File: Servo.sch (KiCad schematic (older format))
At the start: 2 parts, among them P2 CONN_01X03, P3 CONN_01X03

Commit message: añaadido zocalo para sensor de temperatura y primera distribucion sobre la PCB
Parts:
- P2, P3: footprint (none) -> Pin_Headers:Pin_Header_Straight_1x03
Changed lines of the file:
@@
 $Descr User 8268 5846
 encoding utf-8
-Sheet 10 13
+Sheet 10 14
 Title ""
 Date ""
@@
 F 0 "P2" H 2878 2241 50  0000 L CNN
 F 1 "CONN_01X03" H 2878 2150 50  0000 L CNN
-F 2 "" H 2800 2200 50  0000 C CNN
+F 2 "Pin_Headers:Pin_Header_Straight_1x03" H 2800 2200 50  0001 C CNN
 F 3 "" H 2800 2200 50  0000 C CNN
 	1    2800 2200
@@
 F 0 "P3" H 2878 2941 50  0000 L CNN
 F 1 "CONN_01X03" H 2878 2850 50  0000 L CNN
-F 2 "" H 2800 2900 50  0000 C CNN
+F 2 "Pin_Headers:Pin_Header_Straight_1x03" H 2800 2900 50  0001 C CNN
 F 3 "" H 2800 2900 50  0000 C CNN
 	1    2800 2900
@@
 $EndComp
 $Comp
-L +5V #PWR037
+L +5V #PWR039
 U 1 1 5794EAD6
 P 2350 1750
-F 0 "#PWR037" H 2350 1600 50  0001 C CNN
+F 0 "#PWR039" H 2350 1600 50  0001 C CNN
 F 1 "+5V" H 2365 1923 50  0000 C CNN
 F 2 "" H 2350 1750 50  0000 C CNN
@@
 $EndComp
 $Comp
-L GND #PWR038
+L GND #PWR040
 U 1 1 5794EAEE
 P 2450 3350
-F 0 "#PWR038" H 2450 3100 50  0001 C CNN
+F 0 "#PWR040" H 2450 3100 50  0001 C CNN
 F 1 "GND" H 2455 3177 50  0000 C CNN
 F 2 "" H 2450 3350 50  0000 C CNN

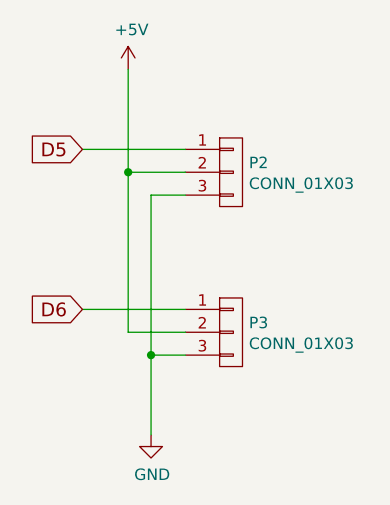
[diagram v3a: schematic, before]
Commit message: ordenar referencias de componentes
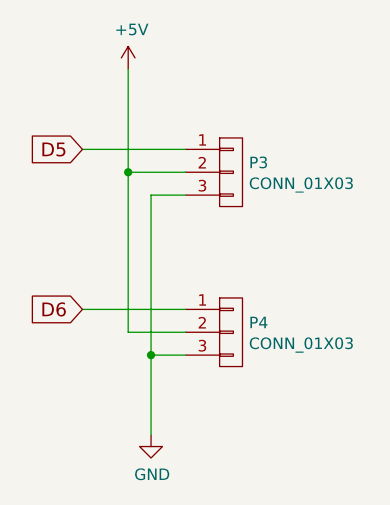
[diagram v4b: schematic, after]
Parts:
- P3: renamed from P2; Fabricante (none) -> TE CONNECTIVITY; Provedor (none) -> TME; Ref (none) -> 4-103321-8; Ref_Proveedor (none) -> 4-103321-8
- P4: renamed from P3; Fabricante (none) -> TE CONNECTIVITY; Provedor (none) -> TME; Ref (none) -> 4-103321-8; Ref_Proveedor (none) -> 4-103321-8
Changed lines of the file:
@@
 $Descr User 8268 5846
 encoding utf-8
-Sheet 10 15
+Sheet 6 15
 Title ""
 Date ""
@@
 $EndDescr
 $Comp
-L CONN_01X03 P2
+L CONN_01X03 P3
 U 1 1 5794EA47
 P 2800 2200
-F 0 "P2" H 2878 2241 50  0000 L CNN
+F 0 "P3" H 2878 2241 50  0000 L CNN
 F 1 "CONN_01X03" H 2878 2150 50  0000 L CNN
 F 2 "Pin_Headers:Pin_Header_Straight_1x03" H 2800 2200 50  0001 C CNN
 F 3 "" H 2800 2200 50  0000 C CNN
+F 4 "TE CONNECTIVITY" H 2800 2200 60  0001 C CNN "Fabricante"
+F 5 "4-103321-8" H 2800 2200 60  0001 C CNN "Ref"
+F 6 "~" H 2800 2200 60  0001 C CNN "Potencia"
+F 7 "~" H 2800 2200 60  0001 C CNN "Tolerancia"
+F 8 "TME" H 2800 2200 60  0001 C CNN "Provedor"
+F 9 "4-103321-8" H 2800 2200 60  0001 C CNN "Ref_Proveedor"
 	1    2800 2200
 	1    0    0    -1
 $EndComp
 $Comp
-L CONN_01X03 P3
+L CONN_01X03 P4
 U 1 1 5794EAA8
 P 2800 2900
-F 0 "P3" H 2878 2941 50  0000 L CNN
+F 0 "P4" H 2878 2941 50  0000 L CNN
 F 1 "CONN_01X03" H 2878 2850 50  0000 L CNN
 F 2 "Pin_Headers:Pin_Header_Straight_1x03" H 2800 2900 50  0001 C CNN
 F 3 "" H 2800 2900 50  0000 C CNN
+F 4 "TE CONNECTIVITY" H 2800 2900 60  0001 C CNN "Fabricante"
+F 5 "4-103321-8" H 2800 2900 60  0001 C CNN "Ref"
+F 6 "~" H 2800 2900 60  0001 C CNN "Potencia"
+F 7 "~" H 2800 2900 60  0001 C CNN "Tolerancia"
+F 8 "TME" H 2800 2900 60  0001 C CNN "Provedor"
+F 9 "4-103321-8" H 2800 2900 60  0001 C CNN "Ref_Proveedor"
 	1    2800 2900
 	1    0    0    -1
 $EndComp
 $Comp
-L +5V #PWR032
+L +5V #PWR18
 U 1 1 5794EAD6
 P 2350 1750
-F 0 "#PWR032" H 2350 1600 50  0001 C CNN
+F 0 "#PWR18" H 2350 1600 50  0001 C CNN
 F 1 "+5V" H 2365 1923 50  0000 C CNN
 F 2 "" H 2350 1750 50  0000 C CNN
@@
 $EndComp
 $Comp
-L GND #PWR033
+L GND #PWR19
 U 1 1 5794EAEE
 P 2450 3350
-F 0 "#PWR033" H 2450 3100 50  0001 C CNN
+F 0 "#PWR19" H 2450 3100 50  0001 C CNN
 F 1 "GND" H 2455 3177 50  0000 C CNN
 F 2 "" H 2450 3350 50  0000 C CNN

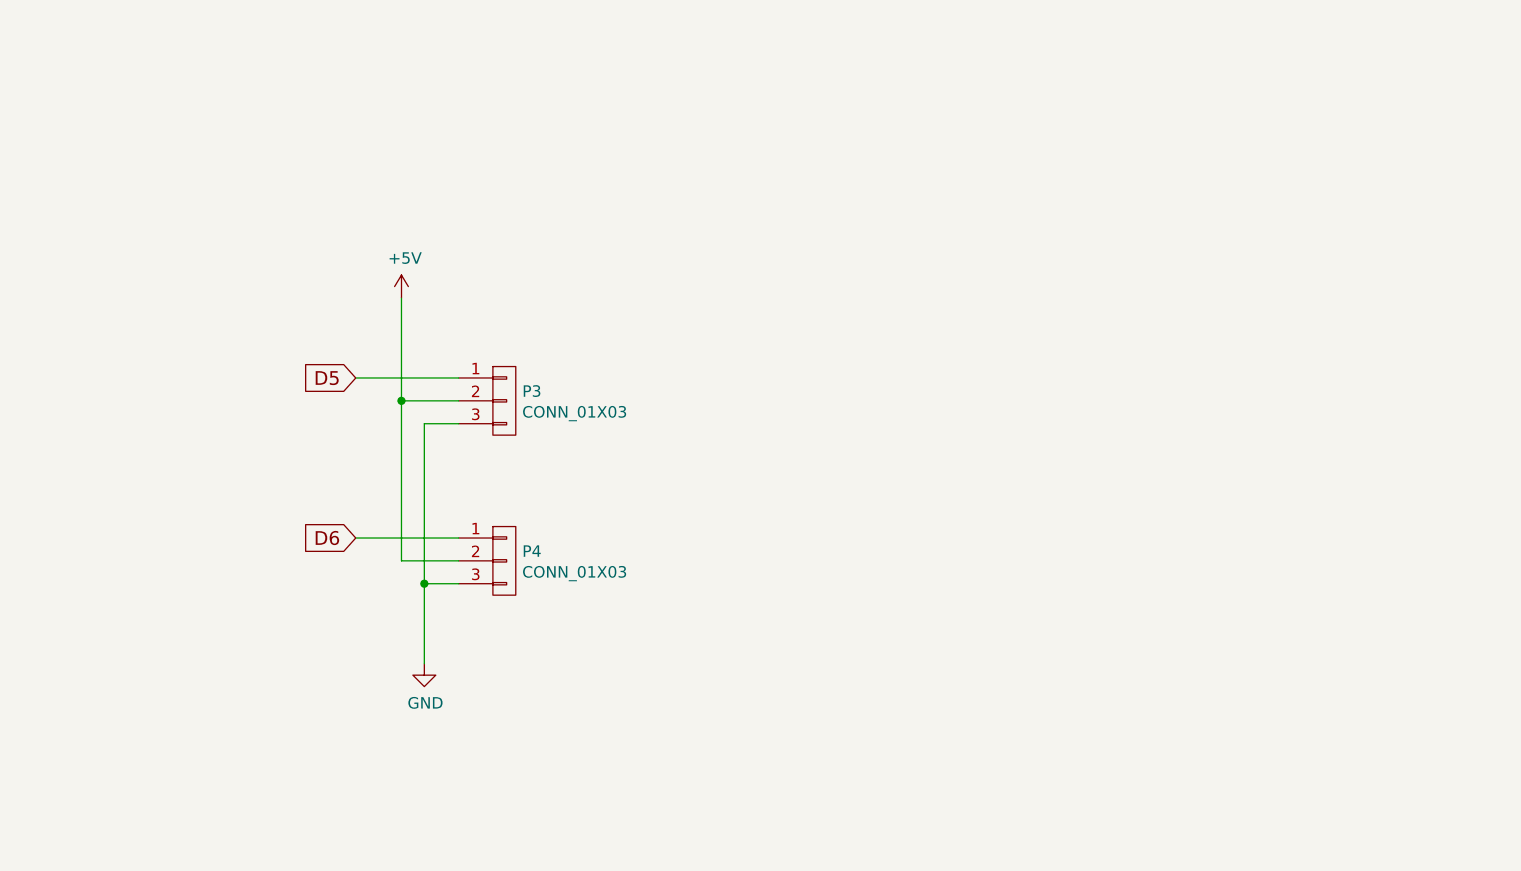
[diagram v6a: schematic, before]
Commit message: añadidos driver para led y conectores para fotodiodos infrarrojos
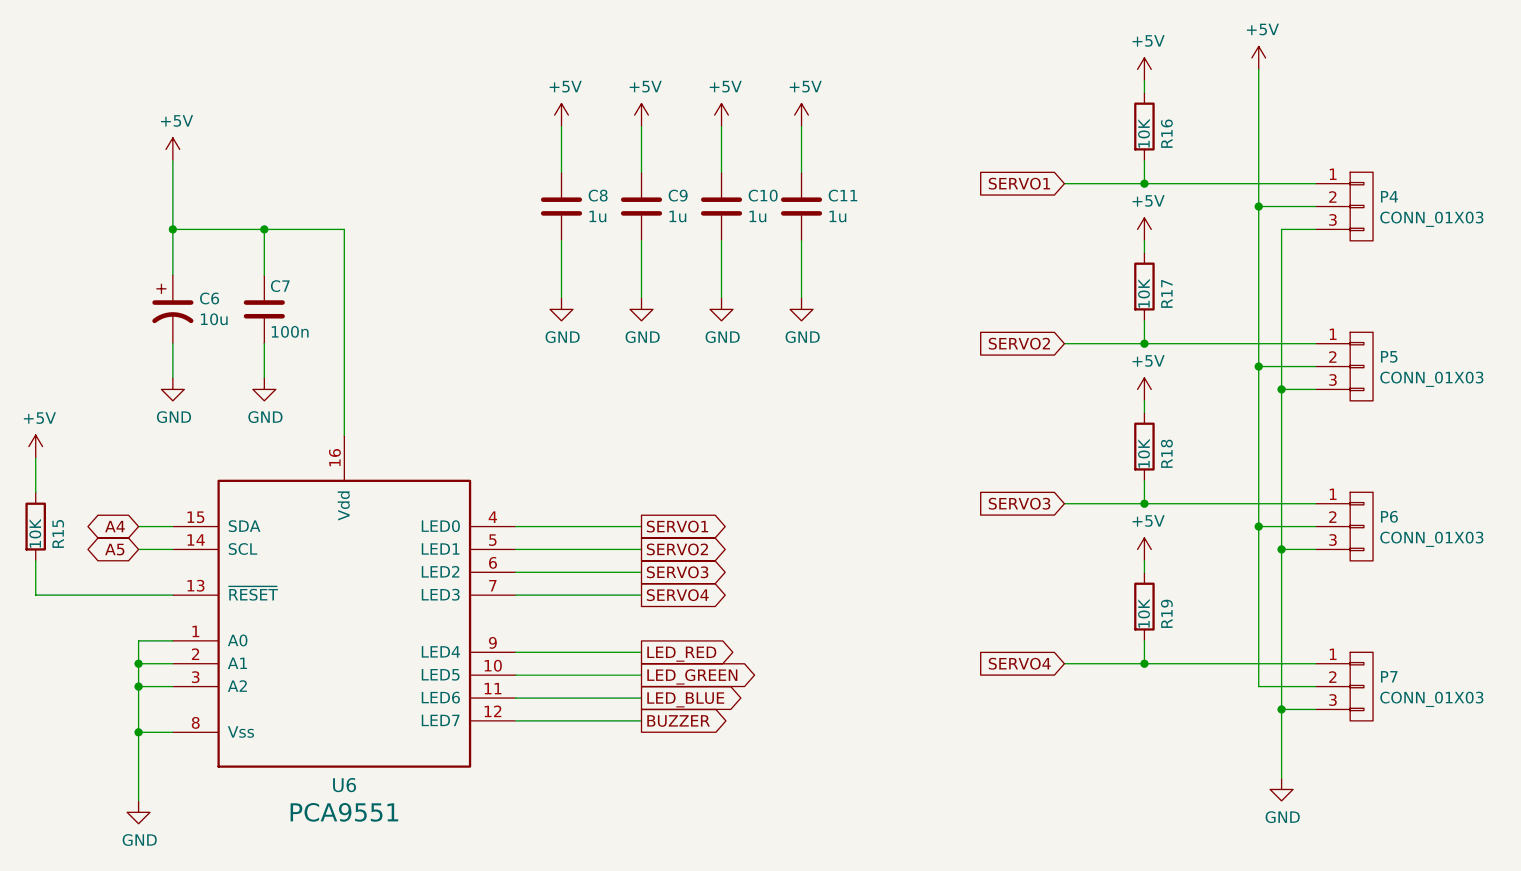
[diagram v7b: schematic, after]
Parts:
- added C10, C11, C8, C9: 1u, Capacitors_SMD:C_0805, symbol C
- added C6: 10u, Capacitors_Tantalum_SMD:Tantalum_Case-A_EIA-3216-18_Reflow, symbol CP1
- added C7: 100n, Capacitors_SMD:C_0805, symbol C
- added P6, P7: CONN_01X03, Pin_Headers:Pin_Header_Straight_1x03, symbol CONN_01X03
- added R15, R16, R17, R18, R19: 10K, Resistencias:R_0805, symbol R
- added U6: PCA9551, Housings_SSOP:TSSOP-16_4.4x5mm_Pitch0.65mm, symbol PCA9551
- renumbered P3 to P4, P4 to P5
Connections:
- net +5V: now also C10.1, C11.1, C6.1, C7.1, C8.1, C9.1, P6.2 (P2), P7.2 (P2), R15.1, R16.1, R17.1, R18.1, R19.1, U6.16 (Vdd)
- net GND: now also C10.2, C11.2, C6.2, C7.2, C8.2, C9.2, P6.3 (P3), P7.3 (P3), U6.1 (A0), U6.2 (A1), U6.3 (A2), U6.8 (Vss)
- net D5 renamed SERVO1
- net SERVO1: now also R16.2, U6.4 (LED0)
- net D6 renamed SERVO2
- net SERVO2: now also R17.2, U6.5 (LED1)
- new net: R15.2, U6.13 (~RESET)
- new net A4: U6.15 (SDA)
- new net A5: U6.14 (SCL)
- new net BUZZER: U6.12 (LED7)
- new net LED_BLUE: U6.11 (LED6)
- new net LED_GREEN: U6.10 (LED5)
- new net LED_RED: U6.9 (LED4)
- new net SERVO3: P6.1 (P1), R18.2, U6.6 (LED2)
- new net SERVO4: P7.1 (P1), R19.2, U6.7 (LED3)
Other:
- moved on the sheet: P4, P5

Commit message: finalizado enrutado provisional
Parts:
- removed C6: 10u, Capacitors_Tantalum_SMD:Tantalum_Case-A_EIA-3216-18_Reflow, symbol CP1
- P4, P5, P6, P7: footprint Pin_Headers:Pin_Header_Straight_1x03 -> Pin_Headers:Pin_Header_Straight_1x03_Pitch2.54mm
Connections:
- net LED_BLUE: now also U6.10 (LED5); no longer U6.11 (LED6)
- net LED_GREEN: now also U6.11 (LED6); no longer U6.10 (LED5)
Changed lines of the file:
@@
 F 0 "P4" H 6628 1391 50  0000 L CNN
 F 1 "CONN_01X03" H 6628 1300 50  0000 L CNN
-F 2 "Pin_Headers:Pin_Header_Straight_1x03" H 6550 1350 50  0001 C CNN
+F 2 "Pin_Headers:Pin_Header_Straight_1x03_Pitch2.54mm" H 6550 1350 50  0001 C CNN
 F 3 "" H 6550 1350 50  0000 C CNN
 F 4 "TE CONNECTIVITY" H 6550 1350 60  0001 C CNN "Fabricante"
@@
 F 0 "P5" H 6628 2091 50  0000 L CNN
 F 1 "CONN_01X03" H 6628 2000 50  0000 L CNN
-F 2 "Pin_Headers:Pin_Header_Straight_1x03" H 6550 2050 50  0001 C CNN
+F 2 "Pin_Headers:Pin_Header_Straight_1x03_Pitch2.54mm" H 6550 2050 50  0001 C CNN
 F 3 "" H 6550 2050 50  0000 C CNN
 F 4 "TE CONNECTIVITY" H 6550 2050 60  0001 C CNN "Fabricante"
@@
 F 0 "P6" H 6628 2791 50  0000 L CNN
 F 1 "CONN_01X03" H 6628 2700 50  0000 L CNN
-F 2 "Pin_Headers:Pin_Header_Straight_1x03" H 6550 2750 50  0001 C CNN
+F 2 "Pin_Headers:Pin_Header_Straight_1x03_Pitch2.54mm" H 6550 2750 50  0001 C CNN
 F 3 "" H 6550 2750 50  0000 C CNN
 F 4 "TE CONNECTIVITY" H 6550 2750 60  0001 C CNN "Fabricante"
@@
 F 0 "P7" H 6628 3491 50  0000 L CNN
 F 1 "CONN_01X03" H 6628 3400 50  0000 L CNN
-F 2 "Pin_Headers:Pin_Header_Straight_1x03" H 6550 3450 50  0001 C CNN
+F 2 "Pin_Headers:Pin_Header_Straight_1x03_Pitch2.54mm" H 6550 3450 50  0001 C CNN
 F 3 "" H 6550 3450 50  0000 C CNN
 F 4 "TE CONNECTIVITY" H 6550 3450 60  0001 C CNN "Fabricante"
@@
 Wire Wire Line
 	2100 1450 2100 2350
-Wire Wire Line
-	1350 1450 2100 1450
-Wire Wire Line
-	1350 1150 1350 1650
-Connection ~ 1350 1450
 $Comp
 L GND #PWR035
@@
 	1    0    0    -1
 $EndComp
+Wire Wire Line
+	1750 2100 1750 1950
+Wire Wire Line
+	2850 2750 3400 2750
+Wire Wire Line
+	2850 2850 3400 2850
+Wire Wire Line
+	2850 2950 3400 2950
+Wire Wire Line
+	2850 3050 3400 3050
+Wire Wire Line
+	2850 3300 3400 3300
+Wire Wire Line
+	2850 3400 3400 3400
+Wire Wire Line
+	2850 3500 3400 3500
+Wire Wire Line
+	2850 3600 3400 3600
+Wire Wire Line
+	1200 3650 1350 3650
+Wire Wire Line
+	1200 3250 1200 3950
 $Comp
 L GND #PWR036
-U 1 1 586D5E3A
-P 1350 2100
-F 0 "#PWR036" H 1350 1850 50  0001 C CNN
-F 1 "GND" H 1355 1927 50  0000 C CNN
-F 2 "" H 1350 2100 50  0000 C CNN
-F 3 "" H 1350 2100 50  0000 C CNN
-	1    1350 2100
-	1    0    0    -1
-$EndComp
-Wire Wire Line
-	1350 1950 1350 2100
-Wire Wire Line
-	1750 2100 1750 1950
-Wire Wire Line
-	2850 2750 3400 2750
-Wire Wire Line
-	2850 2850 3400 2850
-Wire Wire Line
-	2850 2950 3400 2950
-Wire Wire Line
-	2850 3050 3400 3050
-Wire Wire Line
-	2850 3300 3400 3300
-Wire Wire Line
-	2850 3400 3400 3400
-Wire Wire Line
-	2850 3500 3400 3500
-Wire Wire Line
-	2850 3600 3400 3600
-Wire Wire Line
-	1200 3650 1350 3650
-Wire Wire Line
-	1200 3250 1200 3950
-$Comp
-L GND #PWR037
 U 1 1 586D660B
 P 1200 3950
-F 0 "#PWR037" H 1200 3700 50  0001 C CNN
+F 0 "#PWR036" H 1200 3700 50  0001 C CNN
 F 1 "GND" H 1205 3777 50  0000 C CNN
 F 2 "" H 1200 3950 50  0000 C CNN
@@
 Text GLabel 3400 3300 2    50   Output ~ 0
 LED_RED
+Text GLabel 3400 3500 2    50   Output ~ 0
+LED_GREEN
 Text GLabel 3400 3400 2    50   Output ~ 0
-LED_GREEN
-Text GLabel 3400 3500 2    50   Output ~ 0
 LED_BLUE
 Text GLabel 3400 3600 2    50   Output ~ 0
@@
 SERVO4
 $Comp
-L +5V #PWR038
+L +5V #PWR037
 U 1 1 586D839D
-P 1350 1150
-F 0 "#PWR038" H 1350 1000 50  0001 C CNN
-F 1 "+5V" H 1365 1323 50  0000 C CNN
-F 2 "" H 1350 1150 50  0000 C CNN
-F 3 "" H 1350 1150 50  0000 C CNN
-	1    1350 1150
-	1    0    0    -1
-$EndComp
-Wire Wire Line
-	1750 1650 1750 1450
+P 1750 1300
+F 0 "#PWR037" H 1750 1150 50  0001 C CNN
+F 1 "+5V" H 1765 1473 50  0000 C CNN
+F 2 "" H 1750 1300 50  0000 C CNN
+F 3 "" H 1750 1300 50  0000 C CNN
+	1    1750 1300
+	1    0    0    -1
+$EndComp
+Wire Wire Line
+	1750 1300 1750 1650
 Connection ~ 1750 1450
 Wire Wire Line
@@
 	5600 800  5600 850
 $Comp
-L +5V #PWR039
+L +5V #PWR038
 U 1 1 586FF4A2
 P 5600 2900
-F 0 "#PWR039" H 5600 2750 50  0001 C CNN
+F 0 "#PWR038" H 5600 2750 50  0001 C CNN
 F 1 "+5V" H 5615 3073 50  0000 C CNN
 F 2 "" H 5600 2900 50  0000 C CNN
@@
 	5600 2900 5600 2950
 $Comp
-L +5V #PWR040
+L +5V #PWR039
 U 1 1 586FF5CA
 P 5600 800
-F 0 "#PWR040" H 5600 650 50  0001 C CNN
+F 0 "#PWR039" H 5600 650 50  0001 C CNN
 F 1 "+5V" H 5615 973 50  0000 C CNN
 F 2 "" H 5600 800 50  0000 C CNN
@@
 $EndComp
 $Comp
-L +5V #PWR041
+L +5V #PWR040
 U 1 1 586FF689
 P 5600 2200
-F 0 "#PWR041" H 5600 2050 50  0001 C CNN
+F 0 "#PWR040" H 5600 2050 50  0001 C CNN
 F 1 "+5V" H 5615 2373 50  0000 C CNN
 F 2 "" H 5600 2200 50  0000 C CNN
@@
 $EndComp
 $Comp
-L +5V #PWR042
+L +5V #PWR041
 U 1 1 586FF6C1
 P 5600 1500
-F 0 "#PWR042" H 5600 1350 50  0001 C CNN
+F 0 "#PWR041" H 5600 1350 50  0001 C CNN
 F 1 "+5V" H 5615 1673 50  0000 C CNN
 F 2 "" H 5600 1500 50  0000 C CNN
@@
 	750  3050 1350 3050
 $Comp
-L +5V #PWR043
+L +5V #PWR042
 U 1 1 58700007
 P 750 2450
-F 0 "#PWR043" H 750 2300 50  0001 C CNN
+F 0 "#PWR042" H 750 2300 50  0001 C CNN
 F 1 "+5V" H 765 2623 50  0000 C CNN
 F 2 "" H 750 2450 50  0000 C CNN
@@
 	1    0    0    -1
 $EndComp
-$Comp
-L CP1 C6
-U 1 1 58701F31
-P 1350 1800
-F 0 "C6" H 1465 1846 50  0000 L CNN
-F 1 "10u" H 1465 1755 50  0000 L CNN
-F 2 "Capacitors_Tantalum_SMD:Tantalum_Case-A_EIA-3216-18_Reflow" H 1350 1800 50  0001 C CNN
-F 3 "http://www.tme.eu/es/Document/85f84849ee9dc6997647a15c8c95a9d3/taj.pdf" H 1350 1800 50  0001 C CNN
-F 4 "avx" H 1350 1800 60  0001 C CNN "Fabricante"
-F 5 "TAJA106M010RNJ" H 1350 1800 60  0001 C CNN "Ref"
-F 6 "~" H 1350 1800 60  0001 C CNN "Potencia"
-F 7 "~" H 1350 1800 60  0001 C CNN "Tolerancia"
-F 8 "tme" H 1350 1800 60  0001 C CNN "Provedor"
-F 9 "TAJA106M010R" H 1350 1800 60  0001 C CNN "Ref_Proveedor"
-	1    1350 1800
-	1    0    0    -1
-$EndComp
+Wire Wire Line
+	1750 1450 2100 1450
 $EndSCHEMATC
